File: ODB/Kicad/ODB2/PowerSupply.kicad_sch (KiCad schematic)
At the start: 0 parts

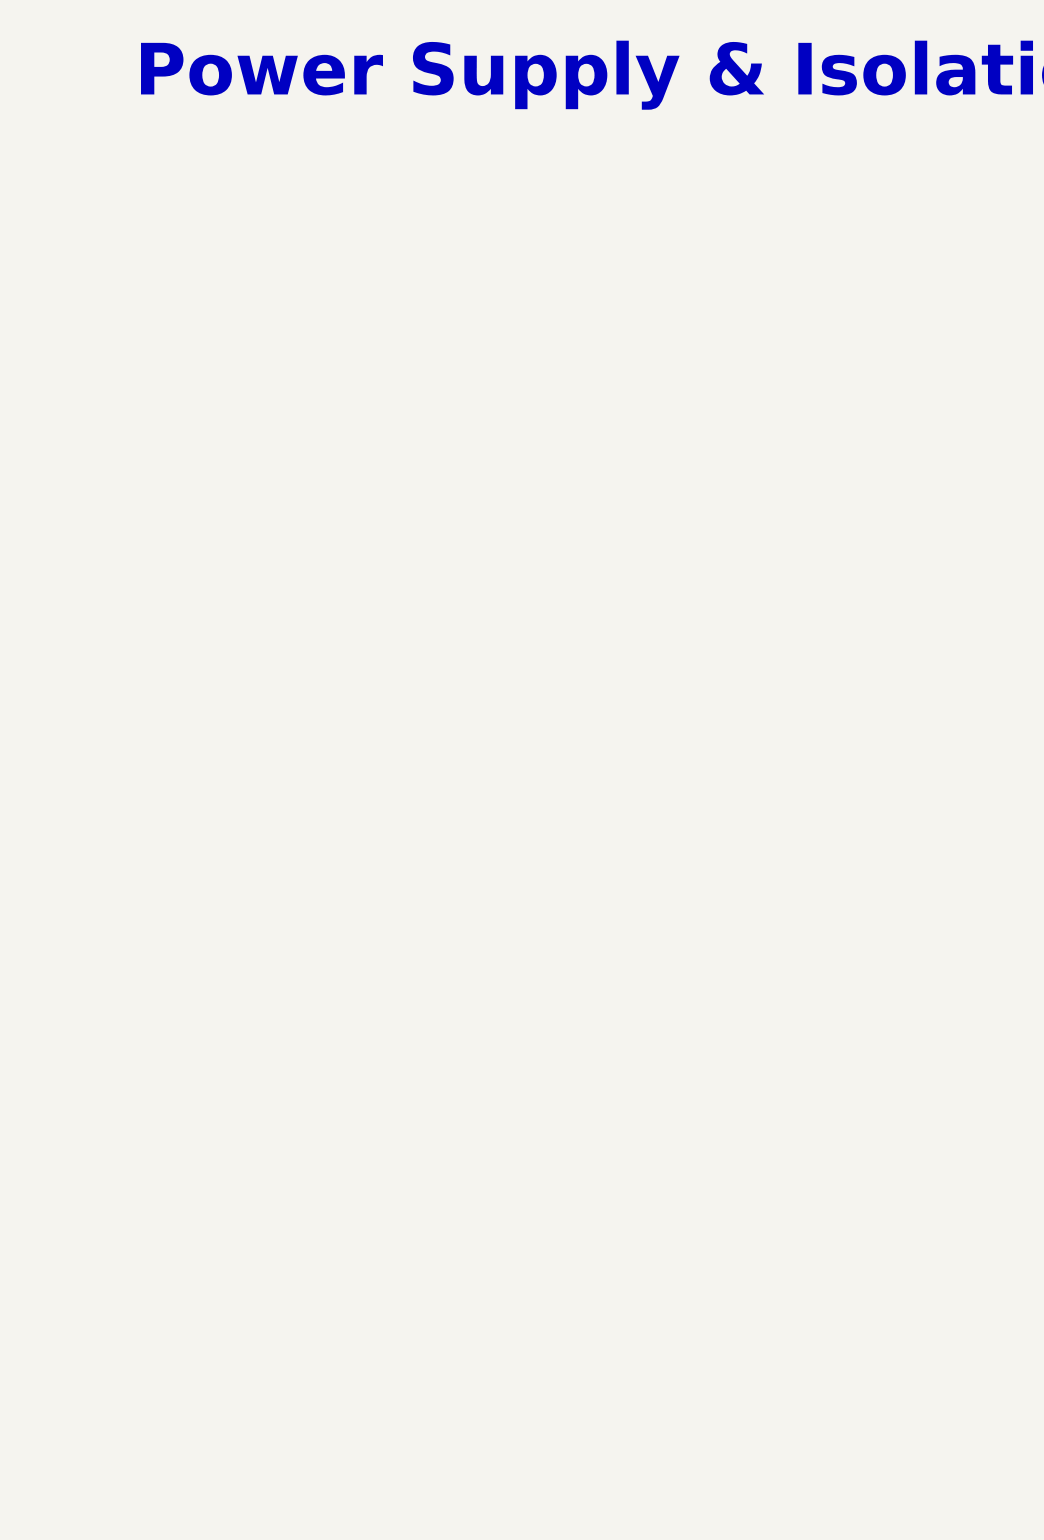
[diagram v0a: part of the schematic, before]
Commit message: Added the power suply
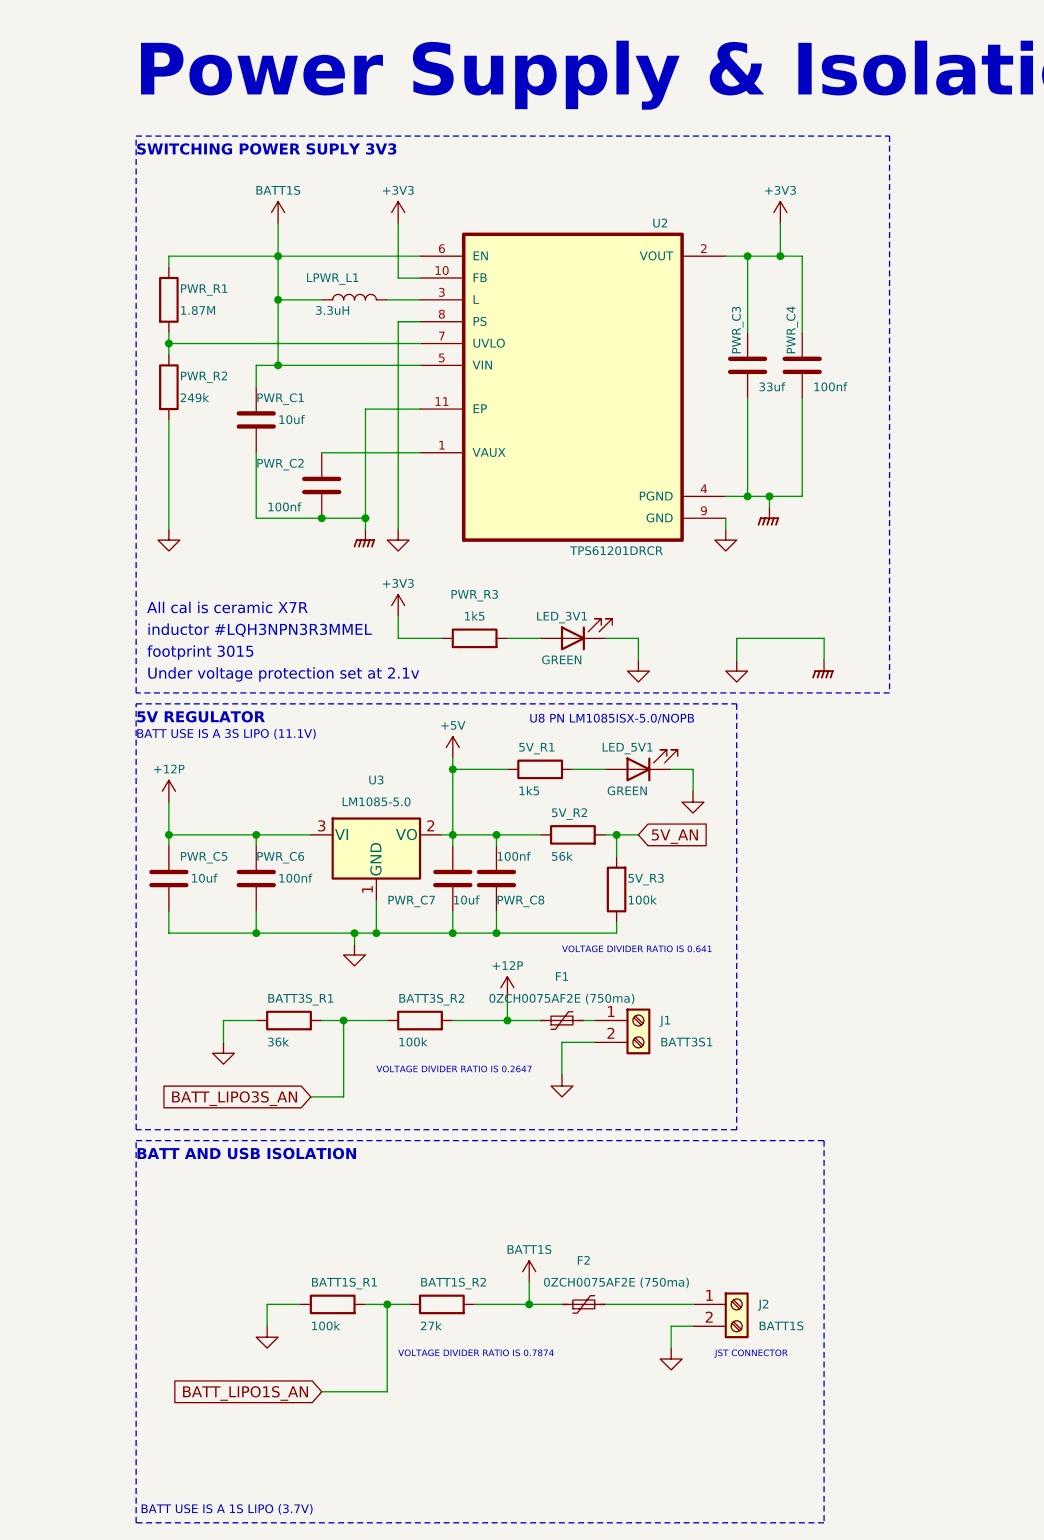
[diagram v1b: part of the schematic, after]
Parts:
- added 5V_R1, PWR_R3: 1k5, Resistor_SMD:R_0805_2012Metric, symbol Device:R
- added 5V_R2: 56k, Resistor_SMD:R_0805_2012Metric, symbol Device:R
- added 5V_R3, BATT1S_R1, BATT3S_R2: 100k, Resistor_SMD:R_0805_2012Metric, symbol Device:R
- added BATT1S_R2: 27k, Resistor_SMD:R_0805_2012Metric, symbol Device:R
- added BATT3S_R1: 36k, Resistor_SMD:R_0805_2012Metric, symbol Device:R
- added F1, F2: 0ZCH0075AF2E (750ma), Fuse:Fuse_1210_3225Metric, symbol Device:Polyfuse_Small
- added J1: BATT3S1, Connector_Wire:SolderWire-2.5sqmm_1x02_P8.8mm_D2.4mm_OD4.4mm, symbol Connector:Screw_Terminal_01x02
- added J2: BATT1S, Connector_JST:JST_XA_B02B-XASK-1_1x02_P2.50mm_Vertical, symbol Connector:Screw_Terminal_01x02
- added LED_3V1, LED_5V1: GREEN, LED_SMD:LED_0805_2012Metric, symbol Device:LED
- added LPWR_L1: 3.3uH, custom_footprints:IND_LQH3NPN3R3MMEL, symbol Device:L
- added PWR_C1, PWR_C5, PWR_C7: 10uf, Capacitor_SMD:C_0805_2012Metric, symbol Device:C
- added PWR_C2, PWR_C4, PWR_C6, PWR_C8: 100nf, Capacitor_SMD:C_0805_2012Metric, symbol Device:C
- added PWR_C3: 33uf, Capacitor_SMD:C_0805_2012Metric, symbol Device:C
- added PWR_R1: 1.87M, Resistor_SMD:R_0805_2012Metric, symbol Device:R
- added PWR_R2: 249k, Resistor_SMD:R_0805_2012Metric, symbol Device:R
- added U2: TPS61201DRCR, Package_SON:VSON-10-1EP_3x3mm_P0.5mm_EP1.65x2.4mm, symbol TPS61201DRCR:TPS61201DRCR
- added U3: LM1085-5.0, Package_TO_SOT_SMD:TO-263-3_TabPin2, symbol Regulator_Linear:LM1085-5.0
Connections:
- new net: PWR_R1.2, PWR_R2.1, U2.7 (UVLO)
- new net: PWR_C2.1, U2.1 (VAUX)
- new net: 5V_R1.2, LED_5V1.2 (A)
- new net: F1.2, J1.1 (Pin_1)
- new net: F2.2, J2.1 (Pin_1)
- new net: LED_3V1.2 (A), PWR_R3.2
- new net: LPWR_L1.2, U2.3 (L)
- new net +12P: BATT3S_R2.2, F1.1, PWR_C5.1, PWR_C6.1, U3.3 (VI)
- new net +3V3: PWR_C3.1, PWR_C4.1, PWR_R3.1, U2.10 (FB), U2.2 (VOUT)
- new net +5V: 5V_R1.1, 5V_R2.1, PWR_C7.1, PWR_C8.1, U3.2 (VO)
- new net 5V_AN: 5V_R2.2, 5V_R3.2
- new net BATT1S: BATT1S_R2.2, F2.1, LPWR_L1.1, PWR_C1.1, PWR_R1.1, U2.5 (VIN), U2.6 (EN)
- new net BATT_LIPO1S_AN: BATT1S_R1.2, BATT1S_R2.1
- new net BATT_LIPO3S_AN: BATT3S_R1.2, BATT3S_R2.1
- new net GND: 5V_R3.1, BATT1S_R1.1, BATT3S_R1.1, J1.2 (Pin_2), J2.2 (Pin_2), LED_3V1.1 (K), LED_5V1.1 (K), PWR_C1.2, PWR_C2.2, PWR_C3.2, PWR_C4.2, PWR_C5.2, PWR_C6.2, PWR_C7.2, PWR_C8.2, PWR_R2.2, U2.11 (EP), U2.4 (PGND), U2.8 (PS), U2.9 (GND), U3.1 (GND)
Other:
- note added: "5V REGULATOR"
- note added: "All cal is ceramic X7R"
- note added: "BATT AND USB ISOLATION"
- note added: "BATT USE IS A 1S LIPO (3.7V)"
- note added: "BATT USE IS A 3S LIPO (11.1V)"
- note added: "JST CONNECTOR"
- note added: "SWITCHING POWER SUPLY 3V3"
- note added: "U8 PN LM1085ISX-5.0/NOPB"
- note added: "Under voltage protection set at 2.1v"
- note added: "VOLTAGE DIVIDER RATIO IS 0.2647"
- note added: "VOLTAGE DIVIDER RATIO IS 0.641"
- note added: "VOLTAGE DIVIDER RATIO IS 0.7874"
- note added: "footprint 3015"
- note added: "inductor #LQH3NPN3R3MMEL"

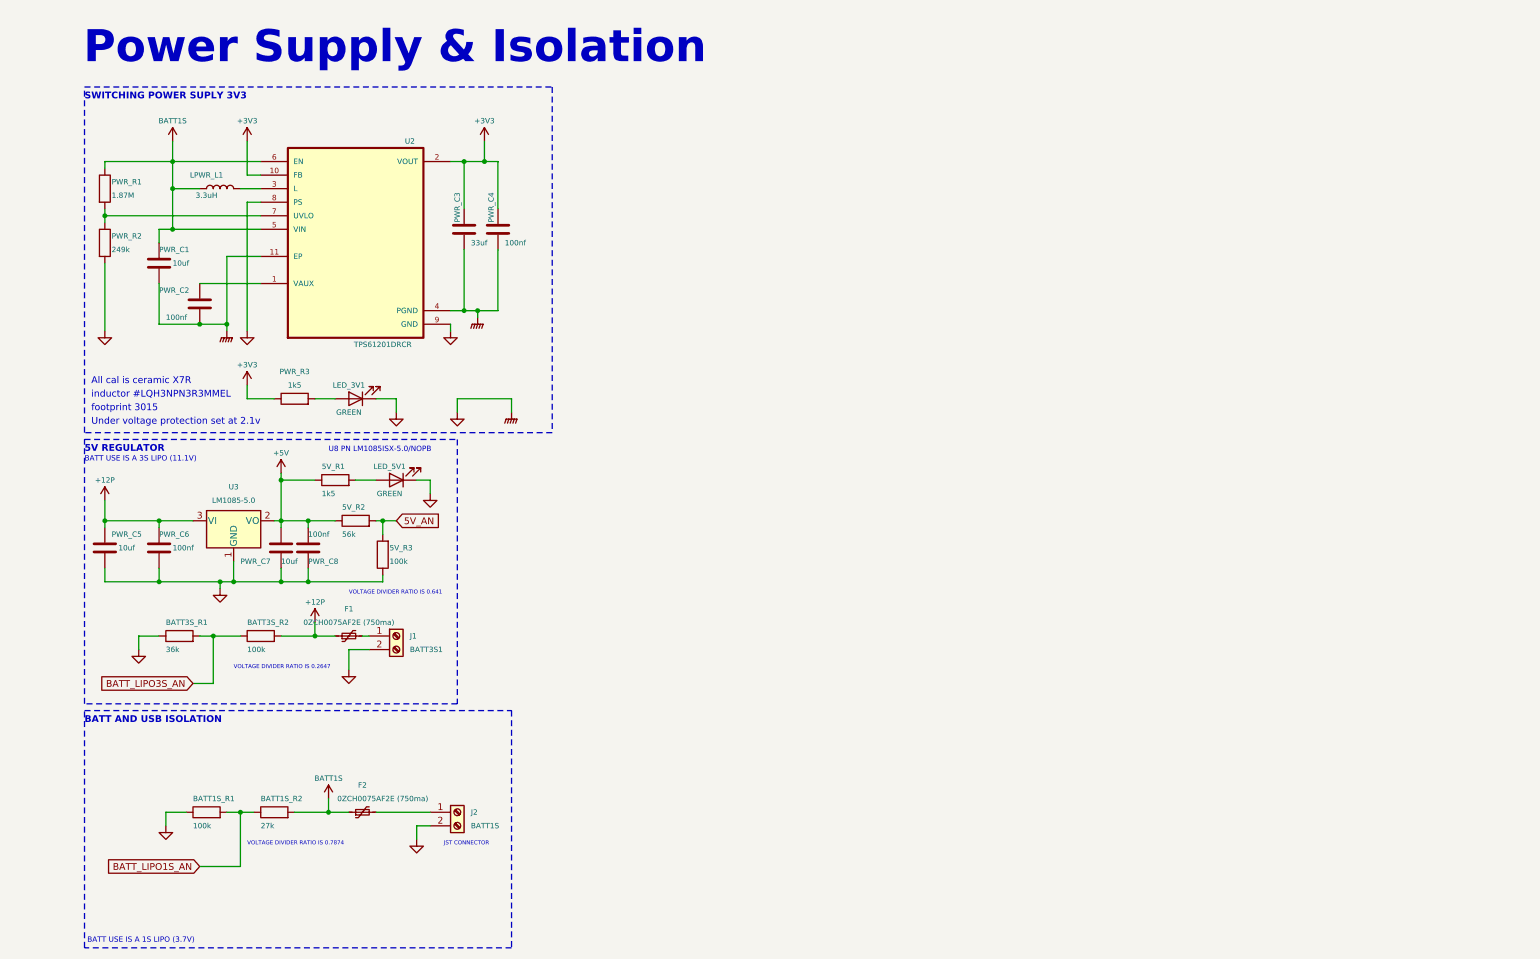
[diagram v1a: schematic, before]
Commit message: Clean up power suply section
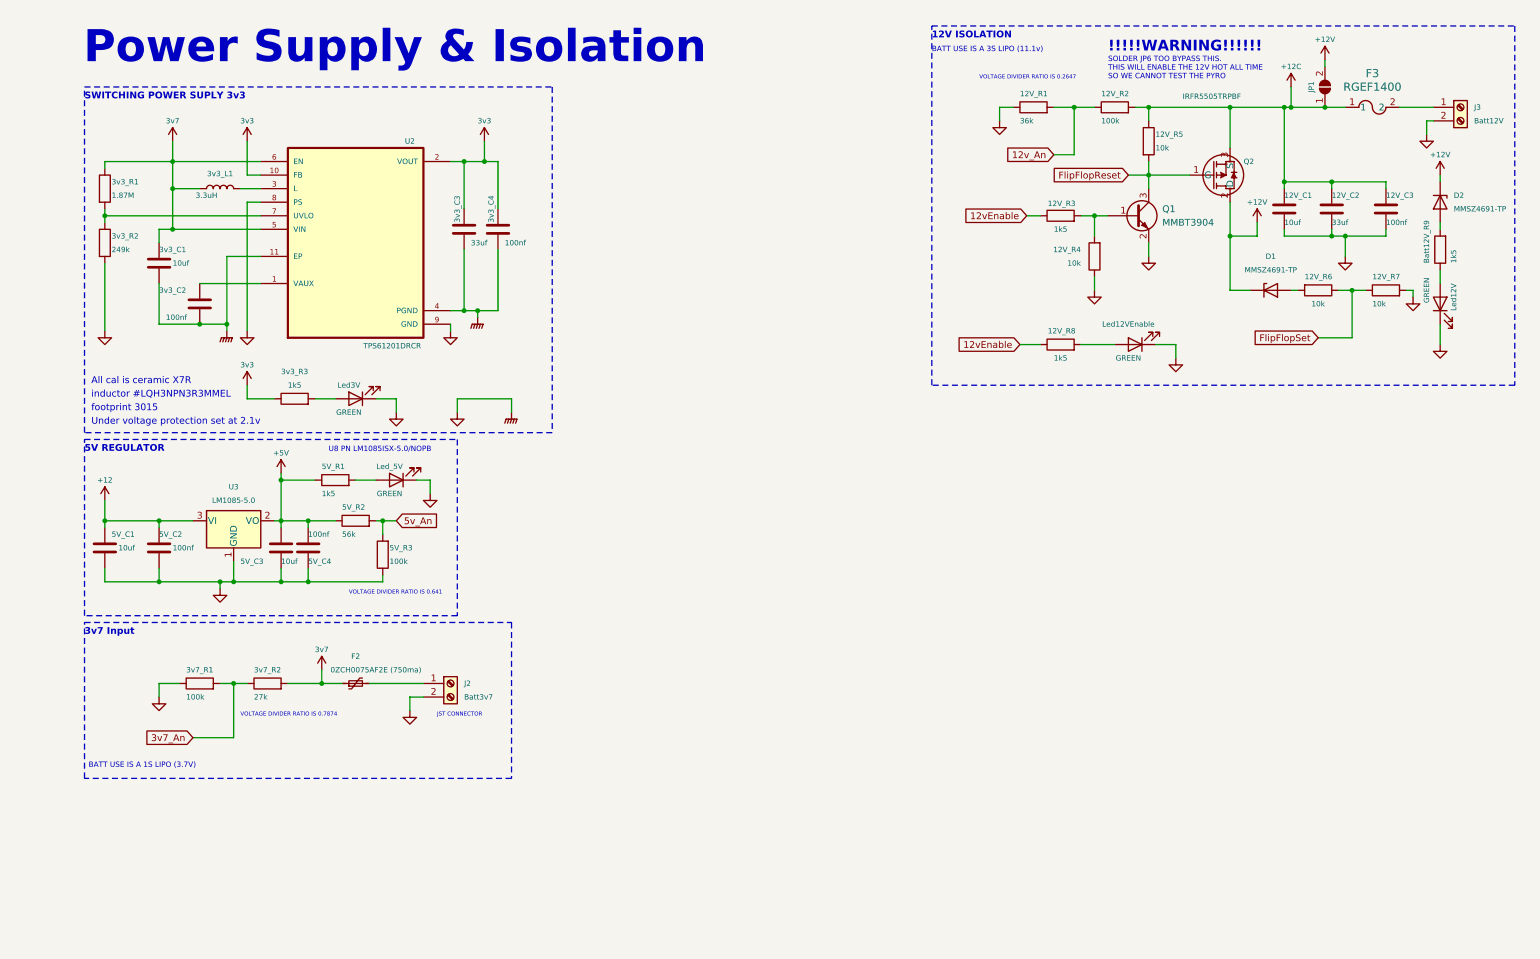
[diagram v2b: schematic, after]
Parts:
- removed BATT3S_R1: 36k, Resistor_SMD:R_0805_2012Metric, symbol Device:R
- removed BATT3S_R2: 100k, Resistor_SMD:R_0805_2012Metric, symbol Device:R
- removed F1: 0ZCH0075AF2E (750ma), Fuse:Fuse_1210_3225Metric, symbol Device:Polyfuse_Small
- removed J1: BATT3S1, Connector_Wire:SolderWire-2.5sqmm_1x02_P8.8mm_D2.4mm_OD4.4mm, symbol Connector:Screw_Terminal_01x02
- added 12V_C1: 10uf, Capacitor_SMD:C_1206_3216Metric, symbol Device:C
- added 12V_C2: 33uf, Capacitor_SMD:C_1206_3216Metric, symbol Device:C
- added 12V_C3: 100nf, Capacitor_SMD:C_1206_3216Metric, symbol Device:C
- added 12V_R1: 36k, Resistor_SMD:R_0805_2012Metric, symbol Device:R
- added 12V_R2: 100k, Resistor_SMD:R_0805_2012Metric, symbol Device:R
- added 12V_R3, 12V_R8, Batt12V_R9: 1k5, Resistor_SMD:R_0805_2012Metric, symbol Device:R
- added 12V_R4, 12V_R5, 12V_R6, 12V_R7: 10k, Resistor_SMD:R_0805_2012Metric, symbol Device:R
- added D1, D2: MMSZ4691-TP, Diode_SMD:D_SOD-123, symbol Diode:BZV55C6V2
- added F3: RGEF1400, FUS_RGEF1400_TYCO_TYC, symbol RGEF1400:RGEF1400
- added J3: Batt12V, Connector_Wire:SolderWire-2.5sqmm_1x02_P8.8mm_D2.4mm_OD4.4mm, symbol Connector:Screw_Terminal_01x02
- added JP1: SolderJumper_2_Open, Jumper:SolderJumper-2_P1.3mm_Open_TrianglePad1.0x1.5mm, symbol Jumper:SolderJumper_2_Open
- added Led12V, Led12VEnable: GREEN, LED_SMD:LED_0805_2012Metric, symbol Device:LED
- added Q1: MMBT3904, Package_TO_SOT_SMD:SOT-23, symbol Transistor_BJT:MMBT3904
- added Q2: IRFR5505TRPBF, custom_footprints:PG-TO252AA_INF, symbol IRFR5505TRPBF:IRFR5505TRPBF
- J2: value BATT1S -> Batt3v7
- renumbered PWR_C1 to 3v3_C1, PWR_C2 to 3v3_C2, PWR_C3 to 3v3_C3, PWR_C4 to 3v3_C4, LPWR_L1 to 3v3_L1, PWR_R1 to 3v3_R1, PWR_R2 to 3v3_R2, PWR_R3 to 3v3_R3, BATT1S_R1 to 3v7_R1, BATT1S_R2 to 3v7_R2, PWR_C5 to 5V_C1, PWR_C6 to 5V_C2, PWR_C7 to 5V_C3, PWR_C8 to 5V_C4, LED_3V1 to Led3V, LED_5V1 to Led_5V
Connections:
- net GND: now also 12V_C1.2, 12V_C2.2, 12V_C3.2, 12V_R1.1, 12V_R4.1, 12V_R7.2, J3.2 (Pin_2), Led12V.1 (K), Led12VEnable.1 (K), Q1.2 (E)
- net +12P renamed +12
- net +3V3 renamed 3v3
- net 5V_AN renamed 5v_An
- net BATT1S renamed 3v7
- net BATT_LIPO1S_AN renamed 3v7_An
- new net: Batt12V_R9.1, Led12V.2 (A)
- new net: Batt12V_R9.2, D2.2 (A)
- new net: 12V_R6.2, D1.2 (A)
- new net: F3.2, J3.1 (Pin_1)
- new net: 12V_R3.2, 12V_R4.2, Q1.1 (B)
- new net: 12V_R8.2, Led12VEnable.2 (A)
- new net +12C: 12V_C1.1, 12V_C2.1, 12V_C3.1, 12V_R2.2, 12V_R5.1, F3.1, JP1.1 (A), Q2.3 (S)
- new net +12V: D1.1 (K), D2.1 (K), JP1.2 (B), Q2.2 (D)
- new net 12vEnable: 12V_R3.1, 12V_R8.1
- new net 12v_An: 12V_R1.2, 12V_R2.1
- new net FlipFlopReset: 12V_R5.2, Q1.3 (C), Q2.1 (G)
- new net FlipFlopSet: 12V_R6.1, 12V_R7.1
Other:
- note added: "!!!!!WARNING!!!!!!"
- note added: "12V ISOLATION"
- note added: "3v7 Input"
- note added: "BATT USE IS A 3S LIPO (11.1v)"
- note added: "SOLDER JP6 TOO BYPASS THIS. THIS WILL ENABLE THE 12V HOT ALL TIME SO WE CANNOT TEST THE PYRO"
- note added: "SWITCHING POWER SUPLY 3v3"
- note removed: "BATT AND USB ISOLATION"
- note removed: "BATT USE IS A 3S LIPO (11.1V)"
- note removed: "SWITCHING POWER SUPLY 3V3"
- moved on the sheet: 3v7_R1, 3v7_R2, F2, J2

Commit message: Added Usb
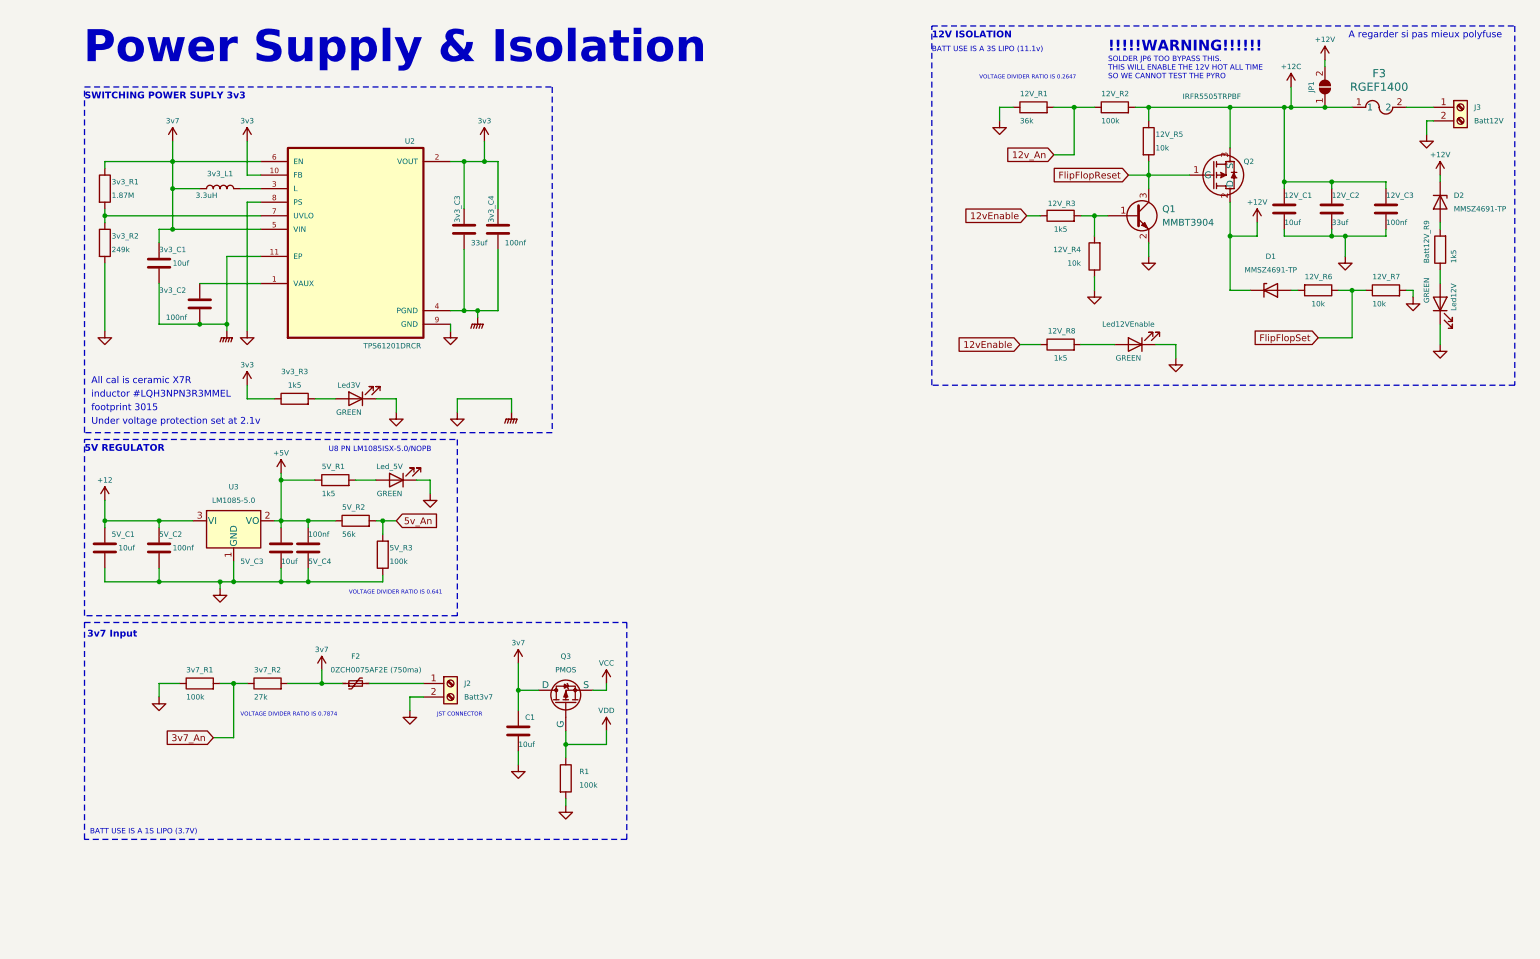
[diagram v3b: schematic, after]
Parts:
- added C1: 10uf, Capacitor_SMD:C_0805_2012Metric, symbol Device:C
- added Q3: PMOS, Package_TO_SOT_SMD:SOT-23-3, symbol Simulation_SPICE:PMOS
- added R1: 100k, Resistor_SMD:R_0805_2012Metric, symbol Device:R
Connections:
- net 3v7: now also C1.1, Q3.3 (D)
- net GND: now also C1.2, R1.2
- new net VCC: Q3.2 (S)
- new net VDD: Q3.1 (G), R1.1
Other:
- note added: "A regarder si pas mieux polyfuse"
- moved on the sheet: F3

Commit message: Fixed label
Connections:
- net +12 renamed 12
- net +12C renamed 12C
- net +12V renamed 12V
- net +5V renamed 5V
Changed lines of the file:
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@@
 			)
 		)
-		(property "Value" "+5V"
+		(property "Value" "5V"
 			(at 52.07 95.25 0)
 			(effects
@@
 			)
 		)
-		(property "Value" "+12C"
+		(property "Value" "12C"
 			(at 241.3 22.86 0)
 			(effects
@@
 			)
 		)
-		(property "Value" "+12V"
+		(property "Value" "12V"
 			(at 247.65 17.78 0)
 			(effects
@@
 			)
 		)
-		(property "Value" "+12V"
+		(property "Value" "12V"
 			(at 234.95 48.26 0)
 			(effects
@@
 			)
 		)
-		(property "Value" "+12"
+		(property "Value" "12"
 			(at 19.05 100.33 0)
 			(effects
@@
 			)
 		)
-		(property "Value" "+12V"
+		(property "Value" "12V"
 			(at 269.24 39.37 0)
 			(effects
